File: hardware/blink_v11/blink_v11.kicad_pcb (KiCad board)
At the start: 2 copper layers, 119 x 92 mm, 176 parts, among them J1 Conn_01x02, J11 KH-BNC50-3511, J12 KH-BNC50-3511, J13 KH-BNC50-3511, J14 Conn_02x16_Odd_Even, J15 Conn_01x01, J16 Conn_01x01, J2 PJ-320D, J3 PJ-320D, J4 KH-BNC50-3511, J5 Conn_01x06_Pin, J6 Conn_01x03, J7 Conn_01x06_Pin, J9 USB_C_Receptacle, Q1 AO3400A, Q2 AO3400A, Q3 2N7002, Q4 2N7002, Q5 2N7002, SW1 SW_SPDT, SW2 SW_Push_4PDT, SW3 SW_Push_4PDT, SW4 SW_Push_4PDT, U1 AMS1117-3.3, U10 TMP112AIDRLR, U11 MAX40200AUK, U12 MAX40200AUK, U13 AMS1117-3.3, U14 SN74LVC1G14DBV, U15 BQ29702DSER, U16 TPS63060, U2 AD8397, U3 M24C02-RMN, U4 STM32F405RGTx, U5 SN74LVC1G14DBV, U6 SN74LVC1G14DBV, U7 CH340C, U8 USBLC6-2P6, U9 MCP73832-2-OT, X1 GTXO-14V (2.048MHz), Y1 16MHz

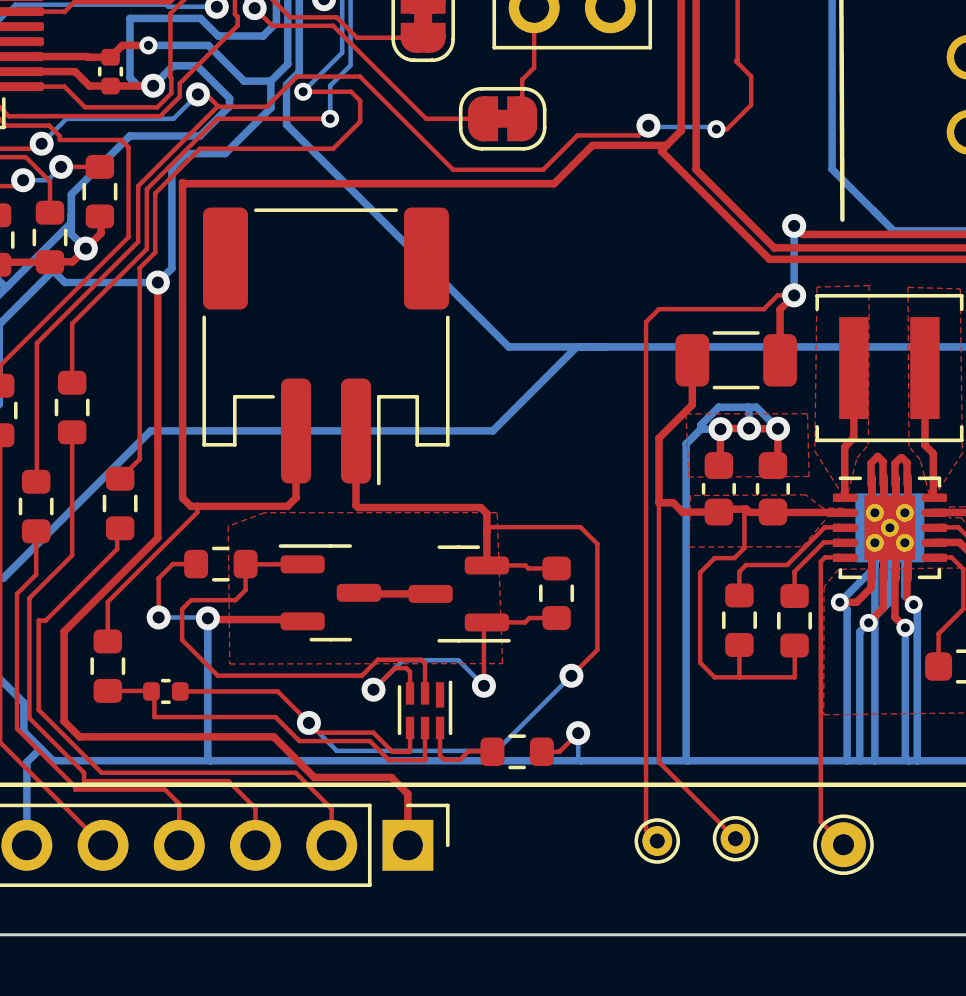
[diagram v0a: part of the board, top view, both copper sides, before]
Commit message: add test points for battery protection
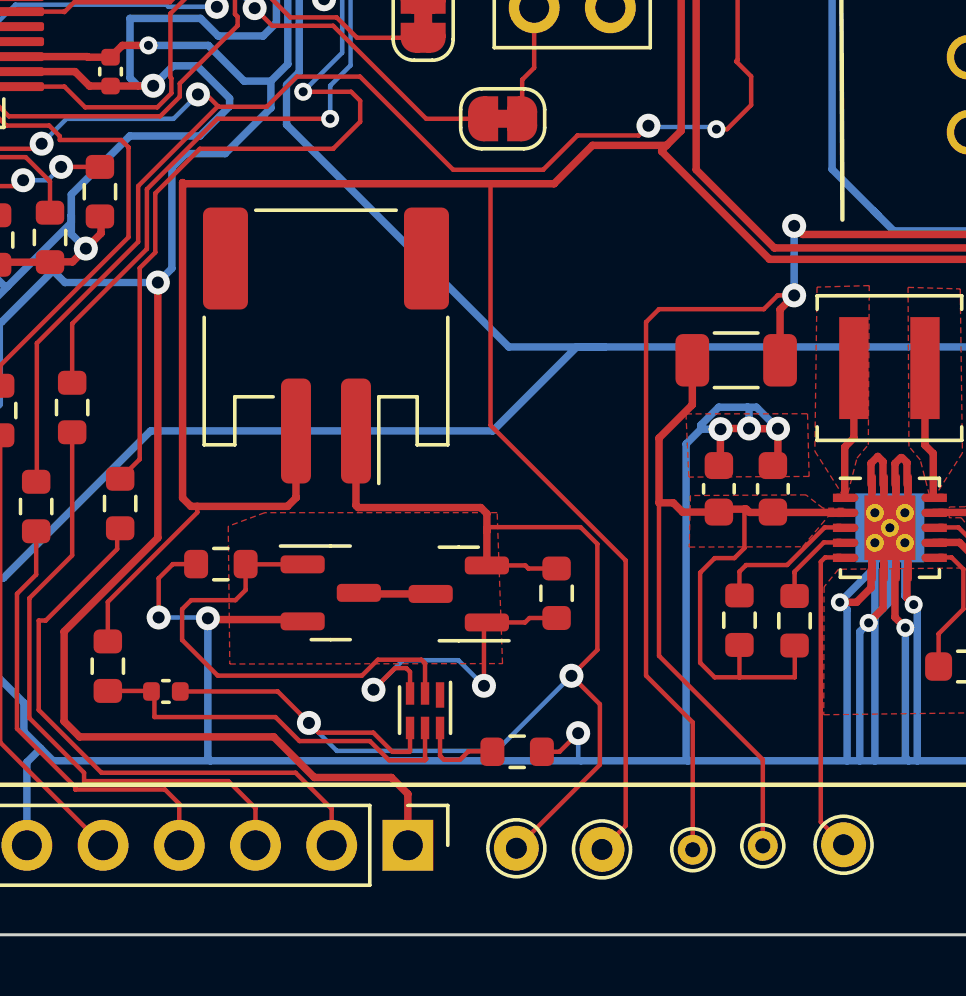
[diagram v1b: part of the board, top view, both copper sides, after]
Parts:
- added TP20: ~, TestPoint:TestPoint_THTPad_D1.5mm_Drill0.7mm, F.Cu at (193.3, 127.2)
- added TP21: ~, TestPoint:TestPoint_THTPad_D1.5mm_Drill0.7mm, F.Cu at (190.4, 127.1)
- moved TP12 1.22 mm to (196.3, 127.2)
- moved TP13 0.94 mm to (198.6, 127.0)
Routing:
- net +BATT: track 133.6 -> 158.0 mm
- net Net-(J1-Pin_1): track 39.2 -> 46.5 mm
- net Net-(SW1-B): track 63.8 -> 64.6 mm
- net /VIN1: track 35.4 -> 36.0 mm

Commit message: swap sync in / pps out
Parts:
- moved TP18 8.02 mm to (143.7, 41.3)
- moved TP14 7.84 mm to (137.5, 41.4)
- moved TP5 7.58 mm to (140.8, 41.3)
- moved TP19 6.54 mm to (149.3, 41.3)
- moved TP2 4.23 mm to (146.7, 41.4)
- moved TP1 3.69 mm to (152.2, 41.4)
- moved J5 1.69 mm to (197.1, 47.4)
- moved JP6 1.24 mm to (204.8, 51.2)
- moved D1 0.98 mm to (208.3, 54.9)
- moved R54 0.96 mm to (198.1, 50.7)
- moved JP5 0.82 mm to (201.3, 51.2)
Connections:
- C25 pad 2: Net-(J12-In) -> Net-(J4-In)
- R23 pad 1: Net-(J4-In) -> Net-(J12-In)
- R24 pad 2: Net-(J12-In) -> Net-(J4-In)
- U6 pad 2: Net-(J4-In) -> Net-(J12-In)
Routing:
- net GND: track 1224.9 -> 1209.2 mm
- net Net-(J12-In): track 46.1 -> 40.1 mm
- net +3.3VA: track 152.0 -> 146.3 mm
- net /VOUT2: track 40.7 -> 35.7 mm
- net +3.3V: track 518.3 -> 513.9 mm
- net Net-(R28-Pad2): track 26.4 -> 22.9 mm
- net +6V: track 228.6 -> 231.9 mm
- net /SCL: track 55.4 -> 52.3 mm, vias 2 -> 0
- net Net-(J4-In): track 103.2 -> 105.7 mm, vias 2 -> 1
- net /USB_RTS: track 50.0 -> 52.5 mm
- net /USB_DTR: track 24.7 -> 22.3 mm
- net Net-(C13-Pad2): track 17.1 -> 18.2 mm
- net /NROW5: track 52.1 -> 51.0 mm
- net /BOOT0: track 98.4 -> 97.5 mm
- net VBUS: track 142.7 -> 141.9 mm
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- added copper zone on B.Cu, net GND

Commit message: clean up
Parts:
- removed FB1: 120Ω@100MHz, Resistor_SMD:R_0603_1608Metric
- removed TP19: ~, TestPoint:TestPoint_THTPad_D1.5mm_Drill0.7mm
- moved R62 4.77 mm to (194.6, 114.5), turned to 90 degrees
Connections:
- C33 pad 1: /VOUT2 -> +3.3VA
- U13 pad 2: /VOUT2 -> +3.3VA
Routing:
- net /VOUT2: track 35.7 -> 0.00 mm, vias 2 -> 0
- net +3.3VA: track 146.3 -> 160.3 mm, vias 8 -> 6
- net +3.3V: track 513.9 -> 505.7 mm
- net Net-(U16-PG): track 10.3 -> 17.3 mm
- net /VIN1: track 36.3 -> 31.6 mm
- net +6V: track 231.9 -> 235.8 mm
- net GND: track 1209.2 -> 1211.3 mm
- net /BOOT0: track 97.5 -> 96.5 mm
- net /USB_RX: track 62.3 -> 61.4 mm
- net /USB_TX: track 61.9 -> 61.1 mm
- net /SDA: track 66.3 -> 67.1 mm
- net /NRST: track 146.0 -> 145.3 mm
- net Net-(U13-VI): track 24.1 -> 23.5 mm
- added copper zone on F.Cu, net +3.3VA
- removed copper zone on F.Cu, net /VOUT2

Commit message: fix up footprints
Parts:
- U16: footprint Package_SON:Texas_S-PWSON-N10_ThermalVias -> blinky_footprints:Texas_S-PWSON-N10_ThermalVias-CJ
- moved C21 3.13 mm to (162.8, 92.0), turned to 180 degrees
- moved C19 0.87 mm to (164.2, 90.0), turned to 0 degrees
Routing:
- net GND: track 1211.3 -> 1203.4 mm, vias 61 -> 62
- net /NRST: track 145.3 -> 141.0 mm
- net /BOOT0: track 96.5 -> 92.3 mm
- net /LEDMB: track 89.3 -> 88.4 mm
- net +6V: track 235.8 -> 236.5 mm
- net +3.3V: track 505.7 -> 506.3 mm

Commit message: clean up
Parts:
- moved R3 1.30 mm to (140.1, 85.6)
- moved C9 0.58 mm to (140.8, 79.8)
- moved R4 0.58 mm to (140.7, 82.0)
- moved J6 0.41 mm to (149.9, 83.7)
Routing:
- net GND: track 1203.4 -> 1200.3 mm
- net /SCL: track 52.3 -> 49.6 mm
- net +3.3V: track 506.3 -> 504.9 mm
- net /SDA: track 67.1 -> 65.7 mm
- net /LED9: track 50.2 -> 51.1 mm
- net /BTN1: track 62.8 -> 62.0 mm
- net PPS_OUT: track 80.6 -> 81.4 mm
- net /AUD_OUT: track 54.6 -> 55.3 mm
- net SYNC_IN: track 60.3 -> 61.0 mm
- net +6V: track 236.5 -> 235.7 mm
- net /AUD_IN: track 45.3 -> 46.0 mm

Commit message: update blink from 6V to 4.7V
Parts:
- R58: value 12K -> 5.6K
- R59: value 120K -> 47K
- R60: value 12K -> 33R0
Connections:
- net +6V renamed +4V
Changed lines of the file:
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@@
   (net 165 "/VIN1")
   (net 166 "Net-(U16-VAUX)")
-  (net 167 "+6V")
+  (net 167 "+4V")
   (net 168 "/FL1")
   (net 169 "/FL2")
@@
       (net 49 "Net-(U1-VI)") (pintype "passive"))
     (pad "2" smd roundrect (at 1.4625 0 270) (size 1.125 1.75) (layers "F.Cu" "F.Paste" "F.Mask") (roundrect_rratio 0.2222222222)
-      (net 167 "+6V") (pintype "passive"))
+      (net 167 "+4V") (pintype "passive"))
     (model "${KICAD6_3DMODEL_DIR}/Resistor_SMD.3dshapes/R_1206_3216Metric.wrl"
       (offset (xyz 0 0 0))
@@
     (descr "Resistor SMD 0603 (1608 Metric), square (rectangular) end terminal, IPC_7351 nominal, (Body size source: IPC-SM-782 page 72, https://www.pcb-3d.com/wordpress/wp-content/uploads/ipc-sm-782a_amendment_1_and_2.pdf), generated with kicad-footprint-generator")
     (tags "resistor")
-    (property "JLCPCB Part #" "C25808")
+    (property "JLCPCB Part #" "C25819")
     (property "Sheetfile" "blink_v11.kicad_sch")
     (property "Sheetname" "")
@@
         (effects (font (size 1 1) (thickness 0.15)))
     )
-    (fp_text value "120K" (at 0 1.43) (layer "F.Fab")
+    (fp_text value "47K" (at 0 1.43) (layer "F.Fab")
         (effects (font (size 1 1) (thickness 0.15)))
     )
@@
       (net 175 "Net-(U16-FB)") (pinfunction "FB") (pintype "input") (solder_mask_margin 0.07) (solder_paste_margin -0.025))
     (pad "9" smd oval (at 1.475 -0.5) (size 0.85 0.28) (layers "F.Cu" "F.Paste" "F.Mask")
-      (net 167 "+6V") (pinfunction "VOUT") (pintype "power_out") (solder_mask_margin 0.07) (solder_paste_margin -0.025))
+      (net 167 "+4V") (pinfunction "VOUT") (pintype "power_out") (solder_mask_margin 0.07) (solder_paste_margin -0.025))
     (pad "9" smd rect (at 1.76 -0.5) (size 0.28 0.28) (layers "F.Cu" "F.Paste" "F.Mask")
-      (net 167 "+6V") (pinfunction "VOUT") (pintype "power_out") (solder_mask_margin 0.07) (solder_paste_margin -0.025))
+      (net 167 "+4V") (pinfunction "VOUT") (pintype "power_out") (solder_mask_margin 0.07) (solder_paste_margin -0.025))
     (pad "10" smd oval (at 1.475 -1) (size 0.85 0.28) (layers "F.Cu" "F.Paste" "F.Mask")
       (net 169 "/FL2") (pinfunction "L2") (pintype "input") (solder_mask_margin 0.07) (solder_paste_margin -0.025))
@@
       (net 1 "+3.3V") (pinfunction "Pin_1") (pintype "passive"))
     (pad "2" thru_hole oval locked (at 2.54 0) (size 1.7 1.7) (drill 1) (layers "*.Cu" "*.Mask")
-      (net 167 "+6V") (pinfunction "Pin_2") (pintype "passive"))
+      (net 167 "+4V") (pinfunction "Pin_2") (pintype "passive"))
     (pad "3" thru_hole oval locked (at 0 2.54) (size 1.7 1.7) (drill 1) (layers "*.Cu" "*.Mask")
       (net 21 "GND") (pinfunction "Pin_3") (pintype "passive"))
@@
     (descr "Resistor SMD 0603 (1608 Metric), square (rectangular) end terminal, IPC_7351 nominal, (Body size source: IPC-SM-782 page 72, https://www.pcb-3d.com/wordpress/wp-content/uploads/ipc-sm-782a_amendment_1_and_2.pdf), generated with kicad-footprint-generator")
     (tags "resistor")
-    (property "JLCPCB Part #" "C22790")
+    (property "JLCPCB Part #" "C23140")
     (property "Sheetfile" "blink_v11.kicad_sch")
     (property "Sheetname" "")
@@
         (effects (font (size 1 1) (thickness 0.15)))
     )
-    (fp_text value "12K" (at 0 1.43) (layer "F.Fab")
+    (fp_text value "33R0" (at 0 1.43) (layer "F.Fab")
         (effects (font (size 1 1) (thickness 0.15)))
     )
@@
       (stroke (width 0.1) (type solid)) (layer "F.Fab"))
     (pad "1" smd roundrect (at -0.825 0 180) (size 0.8 0.95) (layers "F.Cu" "F.Paste" "F.Mask") (roundrect_rratio 0.25)
-      (net 167 "+6V") (pintype "passive"))
+      (net 167 "+4V") (pintype "passive"))
     (pad "2" smd roundrect (at 0.825 0 180) (size 0.8 0.95) (layers "F.Cu" "F.Paste" "F.Mask") (roundrect_rratio 0.25)
       (net 172 "Net-(R59-Pad1)") (pintype "passive"))
@@
       (stroke (width 0.05) (type solid)) (fill none) (layer "F.CrtYd"))
     (pad "1" thru_hole circle (at 0 0) (size 1.5 1.5) (drill 0.7) (layers "*.Cu" "*.Mask")
-      (net 167 "+6V") (pinfunction "1") (pintype "passive"))
+      (net 167 "+4V") (pinfunction "1") (pintype "passive"))
   )
   (footprint "Package_TO_SOT_SMD:SOT-223-3_TabPin2" (layer "F.Cu")
@@
       (stroke (width 0.05) (type solid)) (fill none) (layer "F.CrtYd"))
     (pad "1" thru_hole circle (at 0 0) (size 1 1) (drill 0.5) (layers "*.Cu" "*.Mask")
-      (net 167 "+6V") (pinfunction "1") (pintype "passive"))
+      (net 167 "+4V") (pinfunction "1") (pintype "passive"))
   )
   (footprint "Capacitor_SMD:C_0402_1005Metric" (layer "F.Cu")
@@
       (stroke (width 0.1) (type solid)) (layer "F.Fab"))
     (pad "1" smd roundrect (at -0.95 0 90) (size 1 1.45) (layers "F.Cu" "F.Paste" "F.Mask") (roundrect_rratio 0.25)
-      (net 167 "+6V") (pintype "passive"))
+      (net 167 "+4V") (pintype "passive"))
     (pad "2" smd roundrect (at 0.95 0 90) (size 1 1.45) (layers "F.Cu" "F.Paste" "F.Mask") (roundrect_rratio 0.25)
       (net 21 "GND") (pintype "passive"))
@@
     (descr "Resistor SMD 0603 (1608 Metric), square (rectangular) end terminal, IPC_7351 nominal, (Body size source: IPC-SM-782 page 72, https://www.pcb-3d.com/wordpress/wp-content/uploads/ipc-sm-782a_amendment_1_and_2.pdf), generated with kicad-footprint-generator")
     (tags "resistor")
-    (property "JLCPCB Part #" "C22790")
+    (property "JLCPCB Part #" "C23189")
     (property "Sheetfile" "blink_v11.kicad_sch")
     (property "Sheetname" "")
@@
         (effects (font (size 1 1) (thickness 0.15)))
     )
-    (fp_text value "12K" (at 0 1.43) (layer "F.Fab")
+    (fp_text value "5.6K" (at 0 1.43) (layer "F.Fab")
         (effects (font (size 1 1) (thickness 0.15)))
     )
@@
       (net 155 "Net-(U13-VI)") (pintype "passive"))
     (pad "2" smd roundrect (at 1.4625 0) (size 1.125 1.75) (layers "F.Cu" "F.Paste" "F.Mask") (roundrect_rratio 0.2222222222)
-      (net 167 "+6V") (pintype "passive"))
+      (net 167 "+4V") (pintype "passive"))
     (model "${KICAD6_3DMODEL_DIR}/Resistor_SMD.3dshapes/R_1206_3216Metric.wrl"
       (offset (xyz 0 0 0))
@@
       (stroke (width 0.1) (type solid)) (layer "F.Fab"))
     (pad "1" smd roundrect (at -0.95 0 90) (size 1 1.45) (layers "F.Cu" "F.Paste" "F.Mask") (roundrect_rratio 0.25)
-      (net 167 "+6V") (pintype "passive"))
+      (net 167 "+4V") (pintype "passive"))
     (pad "2" smd roundrect (at 0.95 0 90) (size 1 1.45) (layers "F.Cu" "F.Paste" "F.Mask") (roundrect_rratio 0.25)
       (net 21 "GND") (pintype "passive"))
@@
       (stroke (width 0.05) (type solid)) (fill none) (layer "F.CrtYd"))
     (pad "1" thru_hole circle (at 0 0 180) (size 1 1) (drill 0.5) (layers "*.Cu" "*.Mask")
-      (net 167 "+6V") (pinfunction "1") (pintype "passive"))
+      (net 167 "+4V") (pinfunction "1") (pintype "passive"))
   )
   (footprint "Resistor_SMD:R_0603_1608Metric" (layer "F.Cu")
@@
       (stroke (width 0.1) (type solid)) (layer "F.Fab"))
     (pad "1" smd roundrect (at -0.95 0 90) (size 1 1.45) (layers "F.Cu" "F.Paste" "F.Mask") (roundrect_rratio 0.25)
-      (net 167 "+6V") (pintype "passive"))
+      (net 167 "+4V") (pintype "passive"))
     (pad "2" smd roundrect (at 0.95 0 90) (size 1 1.45) (layers "F.Cu" "F.Paste" "F.Mask") (roundrect_rratio 0.25)
       (net 21 "GND") (pintype "passive"))
@@
     )
   )
-  (zone (net 167) (net_name "+6V") (layer "F.Cu") (hatch edge 0.5)
+  (zone (net 167) (net_name "+4V") (layer "F.Cu") (hatch edge 0.5)
     (priority 12)
     (connect_pads (clearance 0.25))

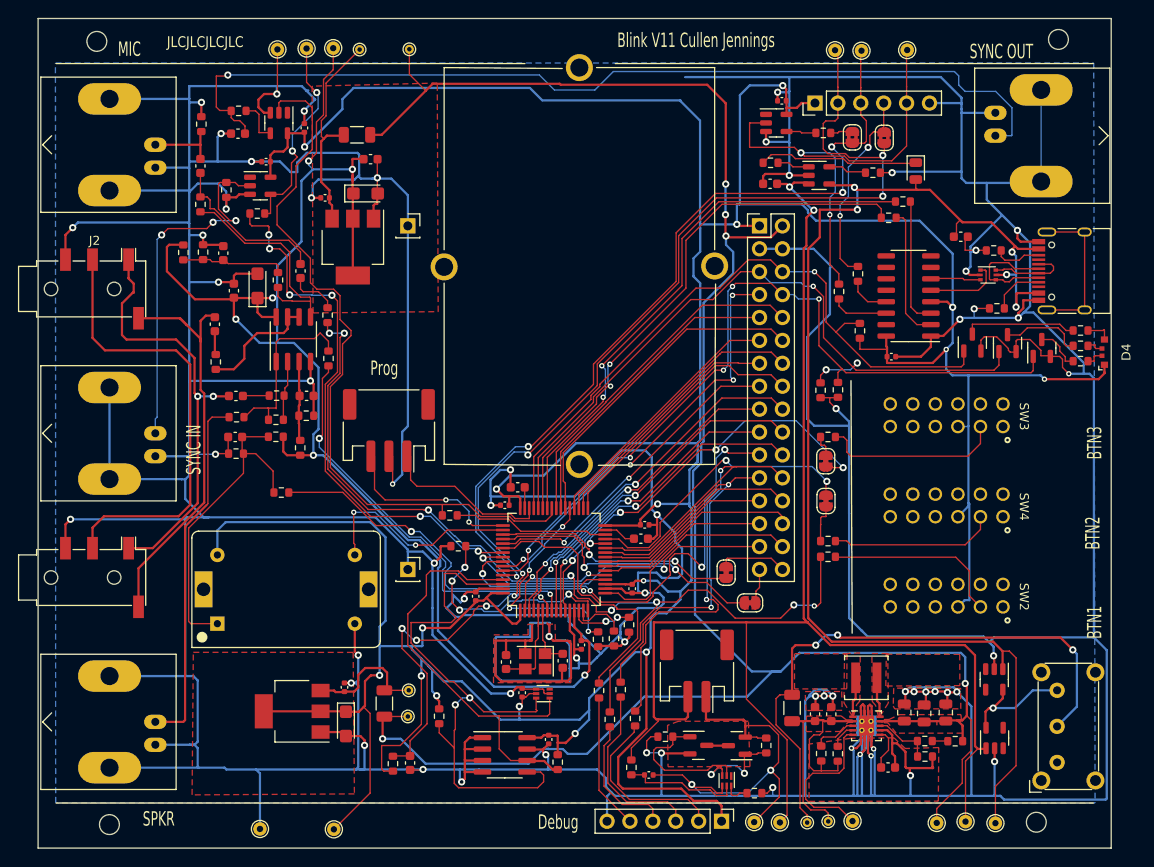
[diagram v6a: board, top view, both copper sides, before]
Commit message: blink V11 hw hardware send to production
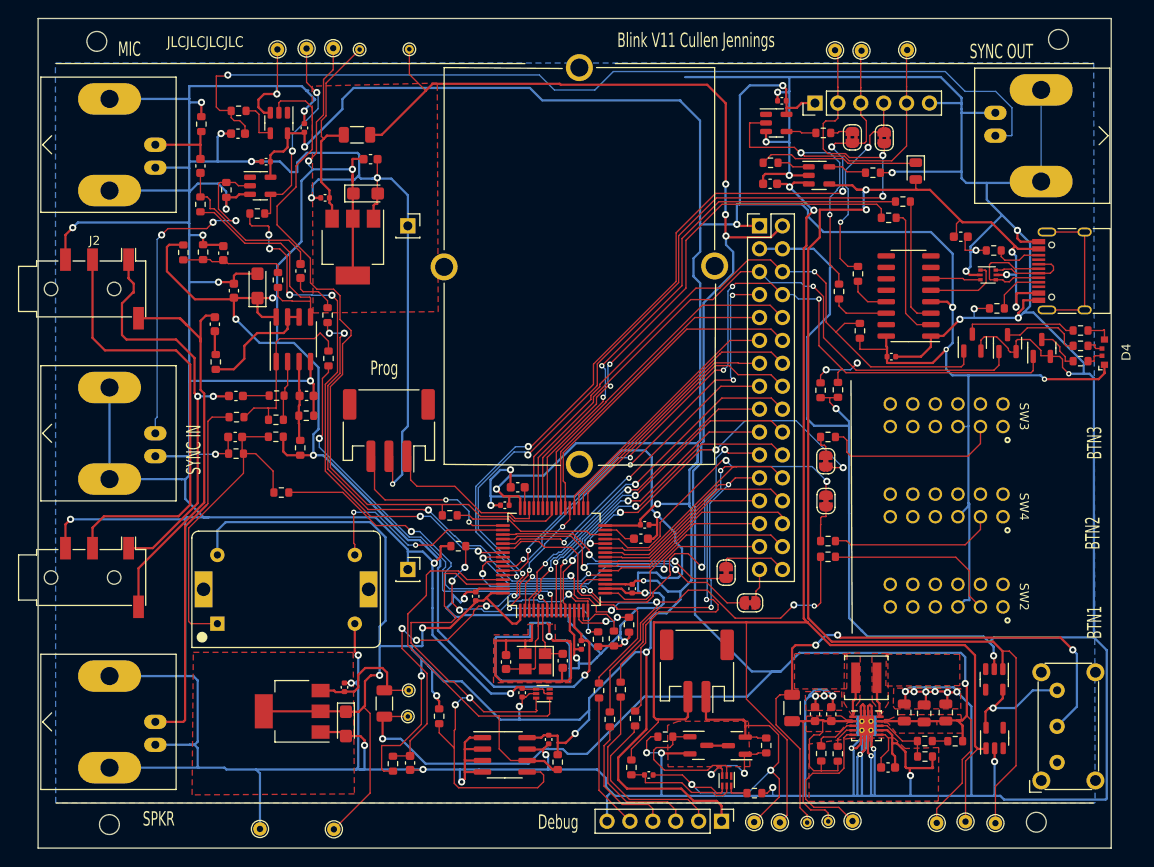
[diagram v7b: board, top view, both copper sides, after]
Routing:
- net VBUS: track 141.9 -> 143.3 mm
- net Net-(J4-In): track 105.7 -> 105.1 mm
